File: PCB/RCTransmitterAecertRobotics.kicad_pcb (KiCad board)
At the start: 2 copper layers, 124.5 x 86.4 mm, 40 parts

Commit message: pcb update
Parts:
- removed H1, H2, H3, H4: MountingHole_Pad, MountingHole:MountingHole_3.2mm_M3
- moved G*** 37.5 mm to (164.1, 110.2)
- moved Bumper2 20.4 mm to (82.3, 80.2)
- moved Bumper4 17.4 mm to (199.6, 81.3)
- moved Bumper3 13.6 mm to (199.6, 70.0)
- moved Bumper1 8.68 mm to (82.3, 70.0)
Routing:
- net /Left Bumper B: track 38.7 -> 18.8 mm
- net /Right Bumper A: track 89.9 -> 105.6 mm
- net /Right Bumper B: track 99.5 -> 109.8 mm
- net /Left Bumper A: track 36.6 -> 32.8 mm
- net /Joy Left Button: track 33.5 -> 34.8 mm
- net /Pot Left: track 73.2 -> 74.4 mm
- net /SCL: track 65.1 -> 64.6 mm
- net /Toggle B: track 73.6 -> 73.1 mm
- net /SCK: track 88.8 -> 88.6 mm, vias 0 -> 1
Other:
- board text added: "V1.03"
- board text removed: "V1.02"

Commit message: updated pcb
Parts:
- moved G*** 34.0 mm to (195.6, 97.5)
- renumbered JST_Connector1 to Battery_Connector1
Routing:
- net /5v: track 393.0 -> 401.2 mm
- net /Joy Left Y: track 63.9 -> 63.0 mm
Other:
- board text added: "Designed By:"
- board text added: "Manufactured By:"
- board text added: "PCBWay"
- board text removed: "+"
- board text removed: "-"
- board text removed: "youtube.com/@aecertrobotics"

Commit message: updated pcb, created gerber
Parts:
- moved Bumper4 1.02 mm to (199.6, 80.3)
- renumbered Battery_Connector1 to Battery1, NRF24 to NRF24L01+PA+LNA1
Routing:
- net /Right Bumper B: track 109.8 -> 110.6 mm
- net /SCK: track 88.6 -> 89.3 mm
- net /Toggle A: track 50.4 -> 51.0 mm
- net /Toggle B: track 73.1 -> 73.6 mm
- net /Right Bumper A: track 105.6 -> 106.1 mm
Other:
- board text added: "Arduino"
- board text added: "RC Transmitter"
- board text added: "Voltage Divider"
- board text added: "aecertrobotics.com"
- board text added: "pcbway.com"
- board text removed: "Arduino RC Transmitter"

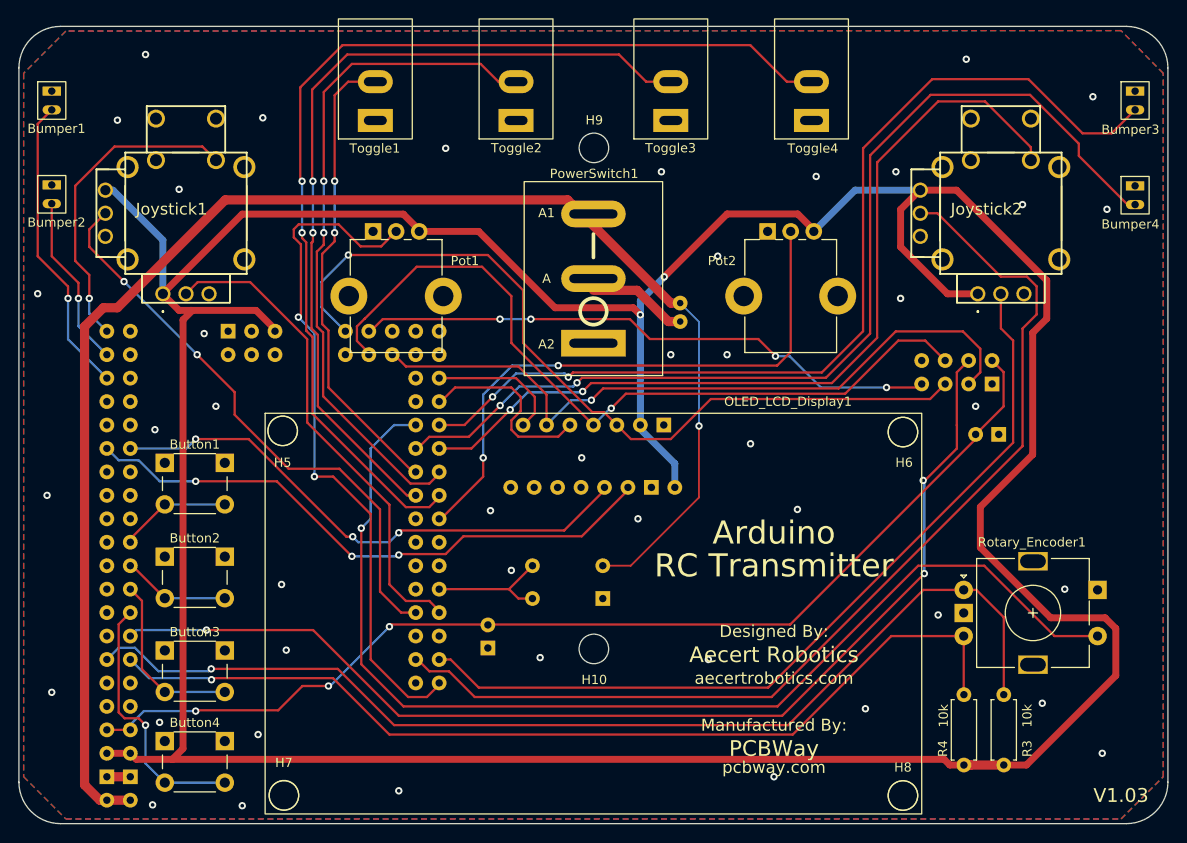
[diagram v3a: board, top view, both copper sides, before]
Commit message: Updated PCB to fix bumper plug clearance
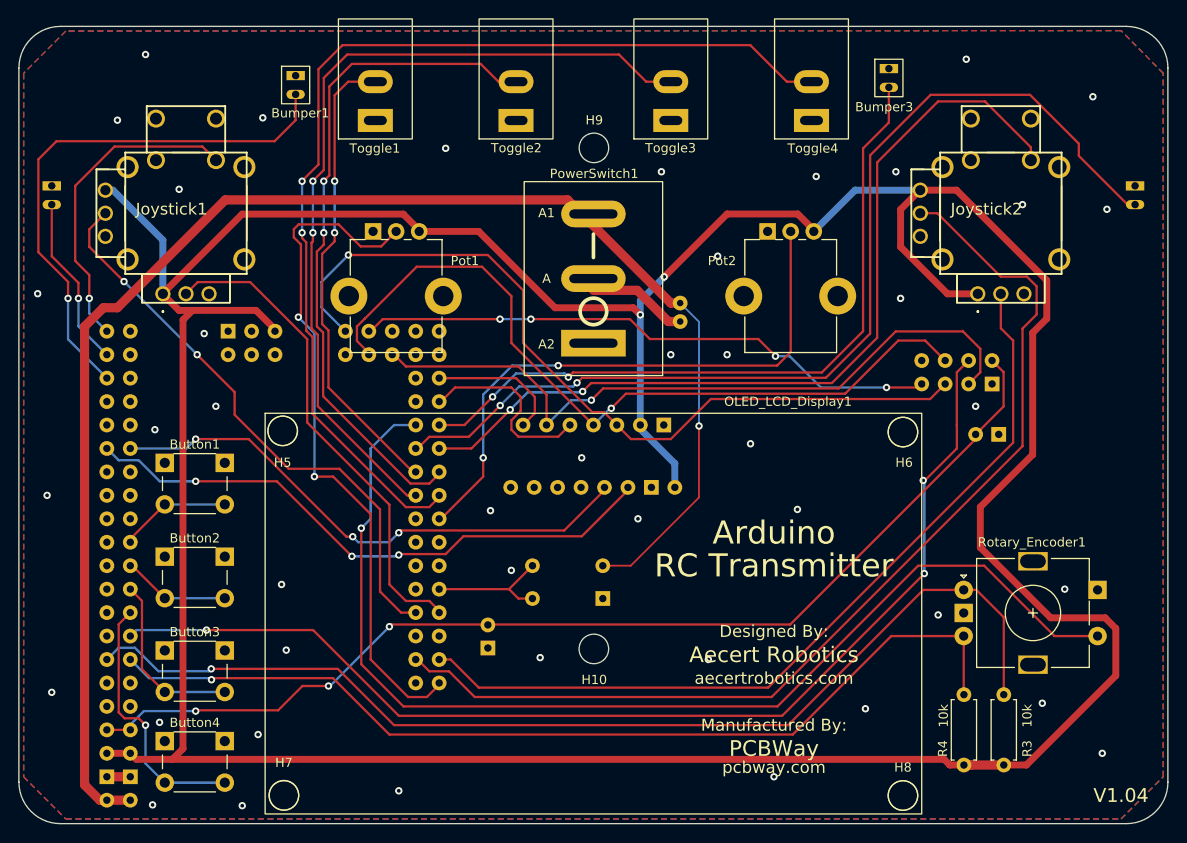
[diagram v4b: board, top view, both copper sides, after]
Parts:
- Bumper2, Bumper4: moved to B.Cu
- moved Bumper3 26.8 mm to (173.0, 67.6)
- moved Bumper1 26.5 mm to (108.7, 68.3)
- moved Bumper2 0.10 mm to (82.3, 80.3), turned to 180 degrees
- turned Bumper4 to 180 degrees
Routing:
- net /Right Bumper A: track 106.1 -> 77.8 mm
- net /Left Bumper A: track 32.8 -> 59.2 mm
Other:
- board text added: "V1.04"
